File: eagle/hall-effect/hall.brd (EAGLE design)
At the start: 20 x 12.7 mm, 3 parts, among them IC1 A1202LH

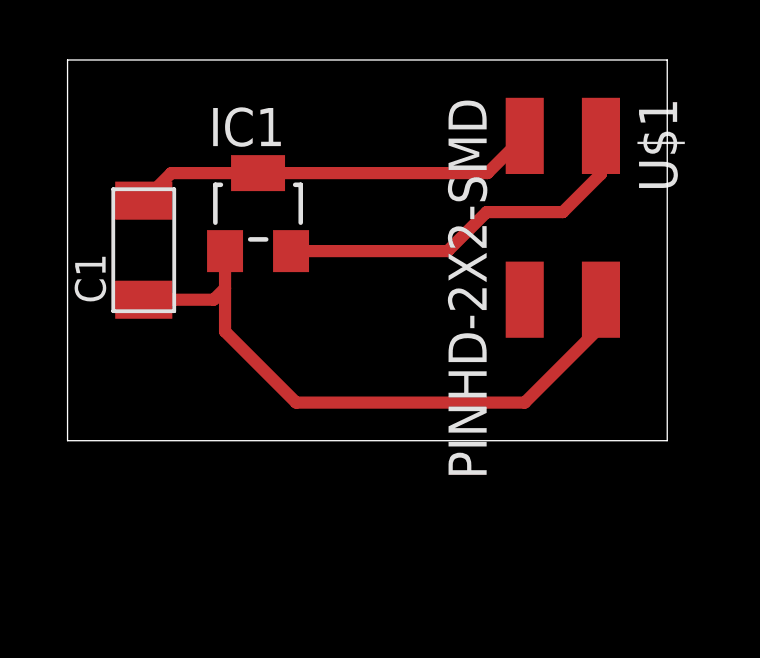
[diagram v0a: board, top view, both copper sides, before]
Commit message: Hall Effect board uses through-hole cables instead of header pins
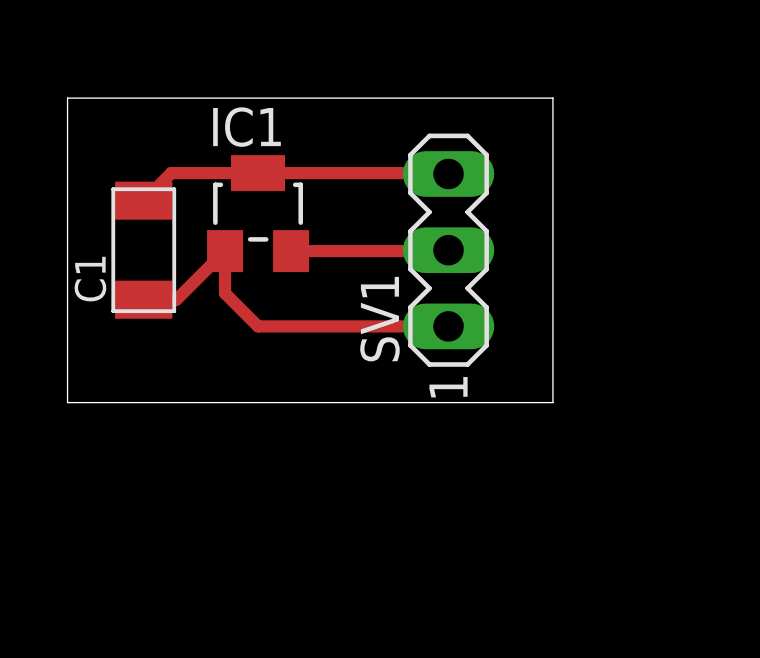
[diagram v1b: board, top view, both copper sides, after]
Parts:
- removed U$1: PINHD-2X2-SMD, fab:2X02SMD
- added SV1: (no value), con-lstb:MA03-1
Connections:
- net N$1: now also SV1.1; no longer U$1.2
- net N$2: now also SV1.2; no longer U$1.1
- net N$3: now also SV1.3; no longer U$1.3
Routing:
- net N$1: track 21.0 -> 12.7 mm
- net N$2: track 12.7 -> 5.26 mm
- net N$3: track 13.6 -> 10.6 mm
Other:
- board size 20 x 12.7 mm -> 16.2 x 10.1 mm
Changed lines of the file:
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@@
 <layer number="27" name="tValues" color="7" fill="1" visible="yes" active="yes"/>
 <layer number="28" name="bValues" color="7" fill="1" visible="yes" active="yes"/>
-<layer number="29" name="tStop" color="7" fill="3" visible="no" active="yes"/>
-<layer number="30" name="bStop" color="7" fill="6" visible="no" active="yes"/>
-<layer number="31" name="tCream" color="7" fill="4" visible="no" active="yes"/>
-<layer number="32" name="bCream" color="7" fill="5" visible="no" active="yes"/>
-<layer number="33" name="tFinish" color="6" fill="3" visible="no" active="yes"/>
-<layer number="34" name="bFinish" color="6" fill="6" visible="no" active="yes"/>
-<layer number="35" name="tGlue" color="7" fill="4" visible="no" active="yes"/>
-<layer number="36" name="bGlue" color="7" fill="5" visible="no" active="yes"/>
-<layer number="37" name="tTest" color="7" fill="1" visible="no" active="yes"/>
-<layer number="38" name="bTest" color="7" fill="1" visible="no" active="yes"/>
+<layer number="29" name="tStop" color="7" fill="3" visible="yes" active="yes"/>
+<layer number="30" name="bStop" color="7" fill="6" visible="yes" active="yes"/>
+<layer number="31" name="tCream" color="7" fill="4" visible="yes" active="yes"/>
+<layer number="32" name="bCream" color="7" fill="5" visible="yes" active="yes"/>
+<layer number="33" name="tFinish" color="6" fill="3" visible="yes" active="yes"/>
+<layer number="34" name="bFinish" color="6" fill="6" visible="yes" active="yes"/>
+<layer number="35" name="tGlue" color="7" fill="4" visible="yes" active="yes"/>
+<layer number="36" name="bGlue" color="7" fill="5" visible="yes" active="yes"/>
+<layer number="37" name="tTest" color="7" fill="1" visible="yes" active="yes"/>
+<layer number="38" name="bTest" color="7" fill="1" visible="yes" active="yes"/>
 <layer number="39" name="tKeepout" color="4" fill="11" visible="yes" active="yes"/>
 <layer number="40" name="bKeepout" color="1" fill="11" visible="yes" active="yes"/>
@@
 <layer number="42" name="bRestrict" color="1" fill="10" visible="yes" active="yes"/>
 <layer number="43" name="vRestrict" color="2" fill="10" visible="yes" active="yes"/>
-<layer number="44" name="Drills" color="7" fill="1" visible="no" active="yes"/>
-<layer number="45" name="Holes" color="7" fill="1" visible="no" active="yes"/>
-<layer number="46" name="Milling" color="3" fill="1" visible="no" active="yes"/>
-<layer number="47" name="Measures" color="7" fill="1" visible="no" active="yes"/>
+<layer number="44" name="Drills" color="7" fill="1" visible="yes" active="yes"/>
+<layer number="45" name="Holes" color="7" fill="1" visible="yes" active="yes"/>
+<layer number="46" name="Milling" color="3" fill="1" visible="yes" active="yes"/>
+<layer number="47" name="Measures" color="7" fill="1" visible="yes" active="yes"/>
 <layer number="48" name="Document" color="7" fill="1" visible="yes" active="yes"/>
 <layer number="49" name="Reference" color="7" fill="1" visible="yes" active="yes"/>
@@
 <board>
 <plain>
-<wire x1="-1.27" y1="66.04" x2="18.72" y2="66.04" width="0" layer="20"/>
-<wire x1="18.72" y1="66.04" x2="18.72" y2="78.73" width="0" layer="20"/>
-<wire x1="18.72" y1="78.73" x2="-1.27" y2="78.73" width="0" layer="20"/>
-<wire x1="-1.27" y1="78.73" x2="-1.27" y2="66.04" width="0" layer="20"/>
+<wire x1="-1.27" y1="67.31" x2="14.91" y2="67.31" width="0" layer="20"/>
+<wire x1="14.91" y1="67.31" x2="14.91" y2="77.46" width="0" layer="20"/>
+<wire x1="14.91" y1="77.46" x2="-1.27" y2="77.46" width="0" layer="20"/>
+<wire x1="-1.27" y1="77.46" x2="-1.27" y2="67.31" width="0" layer="20"/>
 </plain>
 <attributes>
@@
 <attribute name="MF" value="" x="5.08" y="73.66" size="1.778" layer="27" display="off"/>
 </element>
-<element name="U$1" library="fab" package="2X02SMD" value="PINHD-2X2-SMD" x="15.24" y="73.66" rot="R270"/>
 <element name="C1" library="fab" package="C1206FAB" value="CAP-US1206FAB" x="1.27" y="72.39" rot="R90"/>
+<element name="SV1" library="con-lstb" package="MA03-1" value="" x="11.43" y="72.39" rot="R90">
+<attribute name="OC_FARNELL" value="unknown" x="11.43" y="72.39" size="1.778" layer="27" rot="R90" display="off"/>
+<attribute name="OC_NEWARK" value="unknown" x="11.43" y="72.39" size="1.778" layer="27" rot="R90" display="off"/>
+<attribute name="MF" value="" x="11.43" y="72.39" size="1.778" layer="27" rot="R90" display="off"/>
+<attribute name="MPN" value="" x="11.43" y="72.39" size="1.778" layer="27" rot="R90" display="off"/>
+</element>
 </elements>
 <signals>
 <signal name="N$1">
 <contactref element="IC1" pad="1"/>
-<contactref element="U$1" pad="2"/>
-<wire x1="3.98" y1="72.36" x2="3.98" y2="71.12" width="0.4064" layer="1"/>
-<wire x1="3.98" y1="71.12" x2="3.98" y2="69.68" width="0.4064" layer="1"/>
-<wire x1="3.98" y1="69.68" x2="6.35" y2="67.31" width="0.4064" layer="1"/>
-<wire x1="6.35" y1="67.31" x2="13.97" y2="67.31" width="0.4064" layer="1"/>
-<wire x1="13.97" y1="67.31" x2="16.51" y2="69.85" width="0.4064" layer="1"/>
-<wire x1="16.51" y1="69.85" x2="16.51" y2="70.74" width="0.4064" layer="1"/>
 <contactref element="C1" pad="1"/>
-<wire x1="1.27" y1="70.739" x2="3.599" y2="70.739" width="0.4064" layer="1"/>
-<wire x1="3.599" y1="70.739" x2="3.98" y2="71.12" width="0.4064" layer="1"/>
+<contactref element="SV1" pad="1"/>
+<wire x1="1.27" y1="70.739" x2="2.359" y2="70.739" width="0.4064" layer="1"/>
+<wire x1="2.359" y1="70.739" x2="3.98" y2="72.36" width="0.4064" layer="1"/>
+<wire x1="3.98" y1="72.36" x2="3.98" y2="70.95" width="0.4064" layer="1"/>
+<wire x1="3.98" y1="70.95" x2="5.08" y2="69.85" width="0.4064" layer="1"/>
+<wire x1="5.08" y1="69.85" x2="11.43" y2="69.85" width="0.4064" layer="1"/>
 </signal>
 <signal name="N$2">
 <contactref element="IC1" pad="2"/>
-<contactref element="U$1" pad="1"/>
+<contactref element="SV1" pad="2"/>
 <wire x1="6.18" y1="72.36" x2="11.4" y2="72.36" width="0.4064" layer="1"/>
-<wire x1="11.4" y1="72.36" x2="12.7" y2="73.66" width="0.4064" layer="1"/>
-<wire x1="12.7" y1="73.66" x2="15.24" y2="73.66" width="0.4064" layer="1"/>
-<wire x1="15.24" y1="73.66" x2="16.51" y2="74.93" width="0.4064" layer="1"/>
-<wire x1="16.51" y1="74.93" x2="16.51" y2="76.2" width="0.4064" layer="1"/>
+<wire x1="11.4" y1="72.36" x2="11.43" y2="72.39" width="0.4064" layer="1"/>
 </signal>
 <signal name="N$3">
 <contactref element="IC1" pad="3"/>
-<contactref element="U$1" pad="3"/>
-<wire x1="5.08" y1="74.96" x2="12.73" y2="74.96" width="0.4064" layer="1"/>
-<wire x1="12.73" y1="74.96" x2="13.97" y2="76.2" width="0.4064" layer="1"/>
 <contactref element="C1" pad="2"/>
 <wire x1="1.27" y1="74.041" x2="2.189" y2="74.96" width="0.4064" layer="1"/>
 <wire x1="2.189" y1="74.96" x2="5.08" y2="74.96" width="0.4064" layer="1"/>
+<contactref element="SV1" pad="3"/>
+<wire x1="5.08" y1="74.96" x2="11.4" y2="74.96" width="0.4064" layer="1"/>
+<wire x1="11.4" y1="74.96" x2="11.43" y2="74.93" width="0.4064" layer="1"/>
 </signal>
 </signals>
